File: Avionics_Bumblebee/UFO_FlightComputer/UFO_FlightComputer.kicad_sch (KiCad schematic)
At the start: 3 parts, among them U1 RP2040

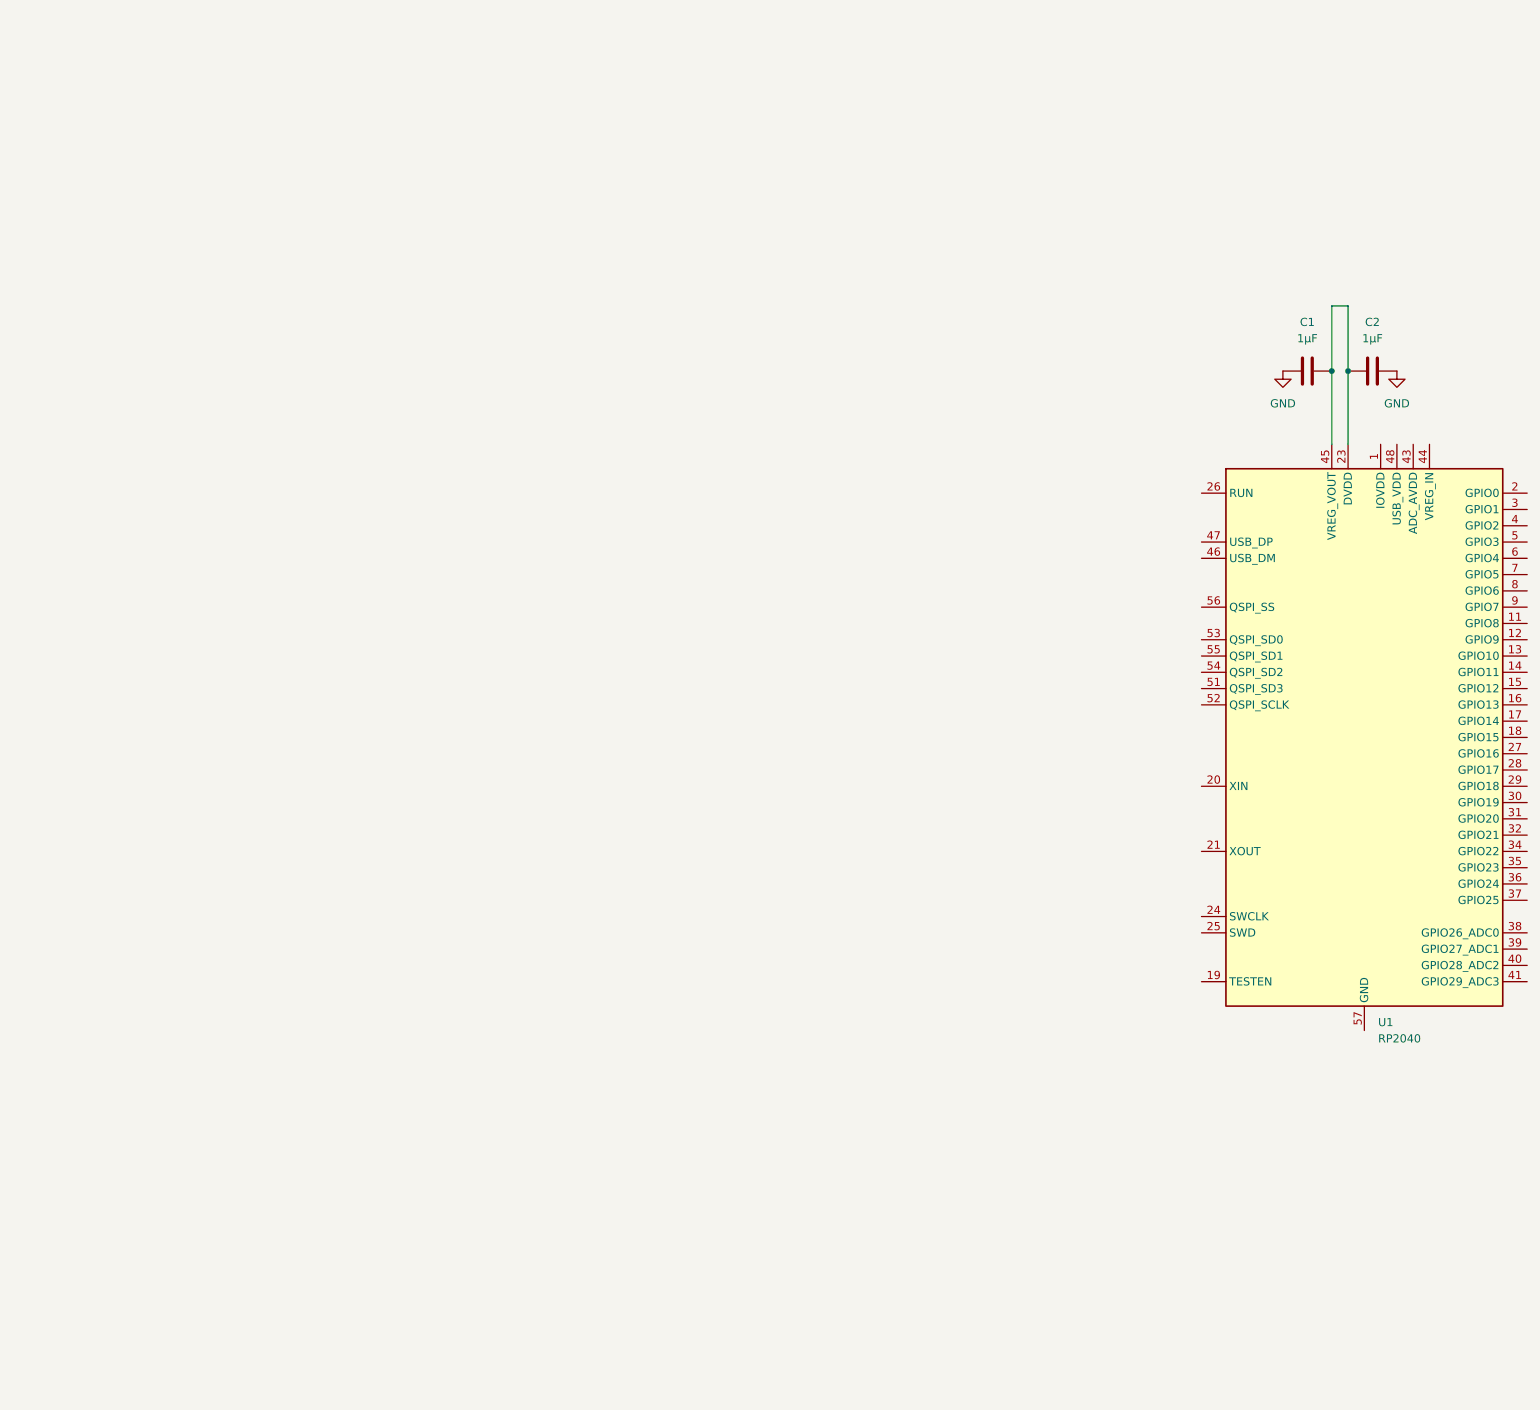
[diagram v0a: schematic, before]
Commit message: pcb design: added usb & power
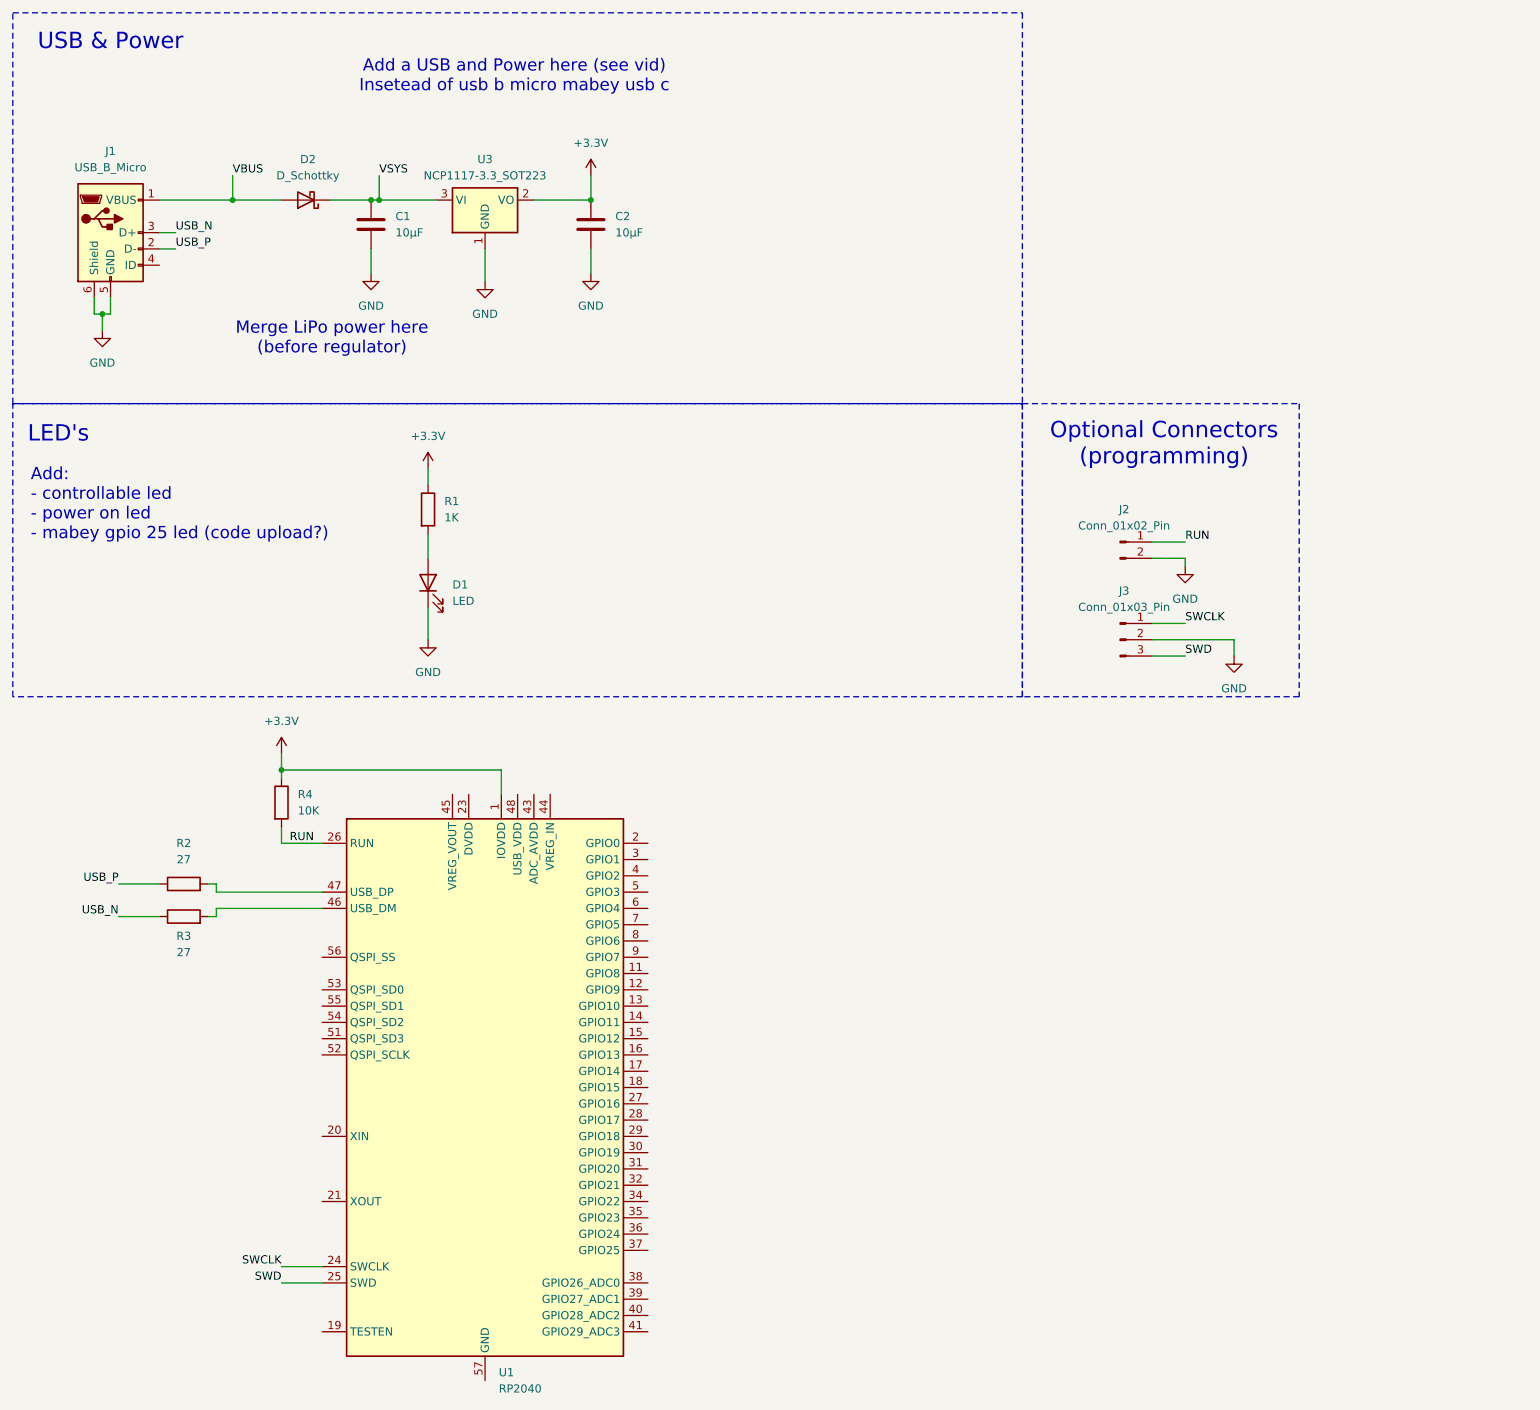
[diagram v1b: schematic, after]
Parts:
- added D1: LED, symbol Device:LED
- added D2: D_Schottky, Diode_SMD:D_SOD-123F, symbol Device:D_Schottky
- added J1: USB_B_Micro, symbol Connector:USB_B_Micro
- added J2: Conn_01x02_Pin, symbol Connector:Conn_01x02_Pin
- added J3: Conn_01x03_Pin, symbol Connector:Conn_01x03_Pin
- added R1: 1K, symbol Device:R
- added R2, R3: 27, symbol Device:R
- added R4: 10K, symbol Device:R
- added U3: NCP1117-3.3_SOT223, Package_TO_SOT_SMD:SOT-223-3_TabPin2, symbol Regulator_Linear:NCP1117-3.3_SOT223
- C1, C2: value 1µF -> 10µF
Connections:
- net GND: now also D1.1 (K), J1.5 (GND), J1.6 (Shield), J2.2 (Pin_2), J3.2 (Pin_2), U3.1 (GND)
- net +3.3V: now reaches U1.1 (IOVDD), U1.10 (IOVDD), U1.22 (IOVDD), U1.33 (IOVDD), U1.42 (IOVDD), U1.49 (IOVDD)
- net +3.3V: now also C2.1, R1.1, R4.1, U3.2 (VO)
- net SWCLK: now reaches U1.24 (SWCLK)
- net SWCLK: now also J3.1 (Pin_1)
- net SWD: now reaches U1.25 (SWD)
- net SWD: now also J3.3 (Pin_3)
- net RUN: now reaches U1.26 (RUN)
- net RUN: now also J2.1 (Pin_1), R4.2
- net at U1.46 (USB_DM): now also R3.2
- net at U1.47 (USB_DP): now also R2.2
- new net: D1.2 (A), R1.2
- new net: U1.23 (DVDD), U1.50 (DVDD)
- new net USB_N: J1.3 (D+), R3.1
- new net USB_P: J1.2 (D-), R2.1
- new net VBUS: D2.2 (A), J1.1 (VBUS)
- new net VSYS: C1.1, D2.1 (K), U3.3 (VI)
- now unconnected: U1.45 (VREG_VOUT)
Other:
- note added: "Add a USB and Power here (see vid) Insetead of usb b micro mabey usb c"
- note added: "Add: - controllable led - power on led - mabey gpio 25 led (code upload?)"
- note added: "LED's"
- note added: "Merge LiPo power here (before regulator)"
- note added: "Optional Connectors (programming)"
- note added: "USB & Power"
- moved on the sheet: U1
